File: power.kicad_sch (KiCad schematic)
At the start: 61 parts, among them J3 Conn_02x05_Odd_Even, T1 net-tie, U1 LMR54410, U2 RT9080-33GJ5, U3 TPS546D24ARVFR, U4 MIC5504

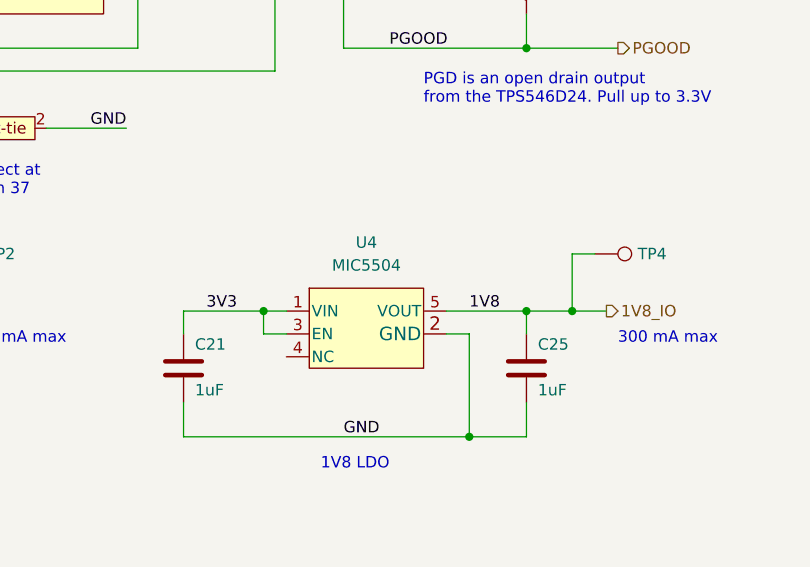
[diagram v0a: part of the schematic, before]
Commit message: finish sch rearrange for BM1368 chain
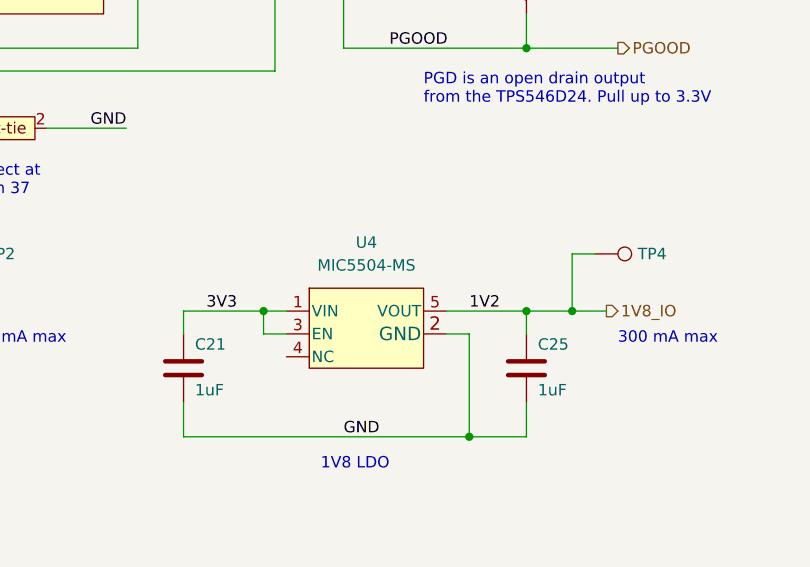
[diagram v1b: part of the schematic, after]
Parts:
- U4: value MIC5504 -> MIC5504-MS; DK 576-4879-1-ND -> C30197547; PARTNO MIC5504-1.8YM5-TR -> MIC5504-1.2YM5-TR-MS
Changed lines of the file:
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@@
 		)
 	)
-	(label "1V8"
+	(label "1V2"
 		(at 196.85 146.05 0)
 		(fields_autoplaced yes)
@@
 			)
 		)
-		(property "Value" "MIC5504"
+		(property "Value" "MIC5504-MS"
 			(at 185.42 140.97 0)
 			(effects
@@
 			)
 		)
-		(property "Datasheet" "https://www.digikey.com/en/products/detail/microchip-technology/MIC5504-1-8YM5-TR/5209404"
+		(property "Datasheet" "https://atta.szlcsc.com/upload/public/pdf/source/20240802/A85BC169CD94B58DB0326F7C46D76917.pdf"
 			(at 177.8 147.32 0)
 			(effects
@@
 			)
 		)
-		(property "DK" "576-4879-1-ND"
+		(property "DK" "C30197547"
 			(at 185.42 147.32 0)
 			(effects
@@
 			)
 		)
-		(property "PARTNO" "MIC5504-1.8YM5-TR"
+		(property "PARTNO" "MIC5504-1.2YM5-TR-MS"
 			(at 185.42 147.32 0)
 			(effects

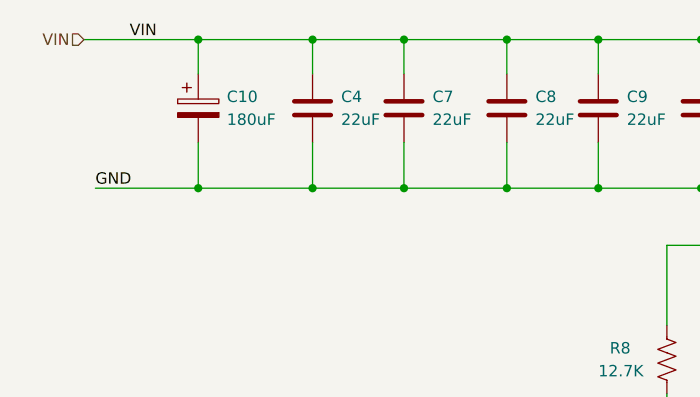
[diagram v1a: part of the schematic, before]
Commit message: Add TVS protection to avoid sudden current which may damage the TPS power regulator
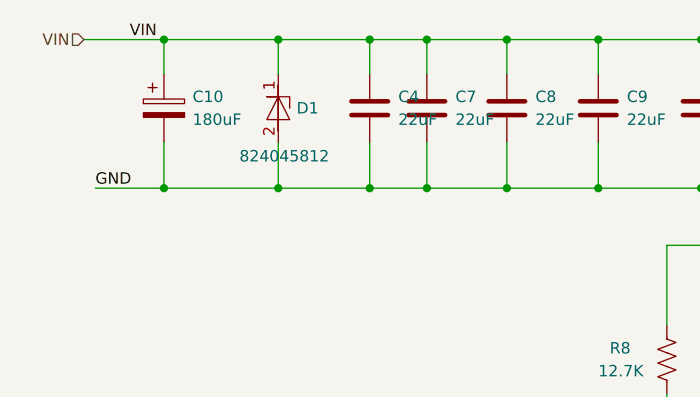
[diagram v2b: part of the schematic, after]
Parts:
- added D1: 824045812, bitaxe:824045812, symbol bitaxe:824045812
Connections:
- net GND: now also D1.2 (GND)
- net VIN: now also D1.1 (I/O)
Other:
- moved on the sheet: C10, C4, C7

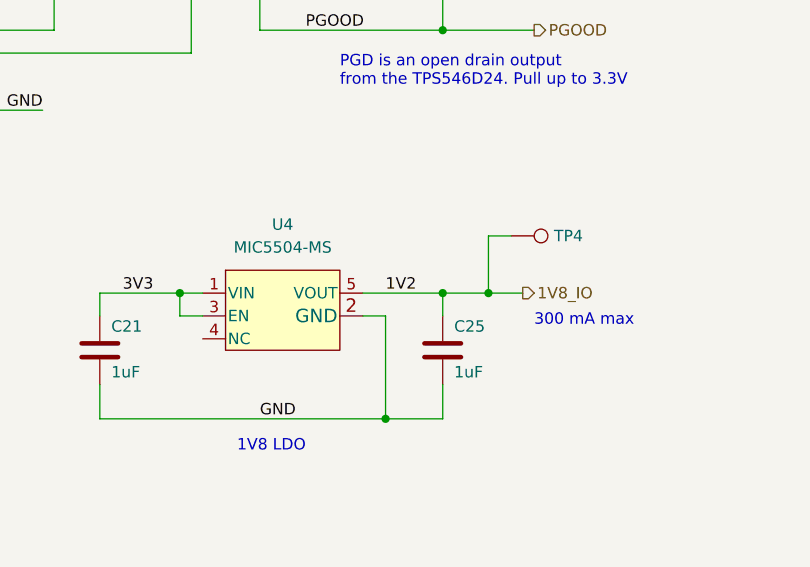
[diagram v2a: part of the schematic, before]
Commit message: Reset to 1V8
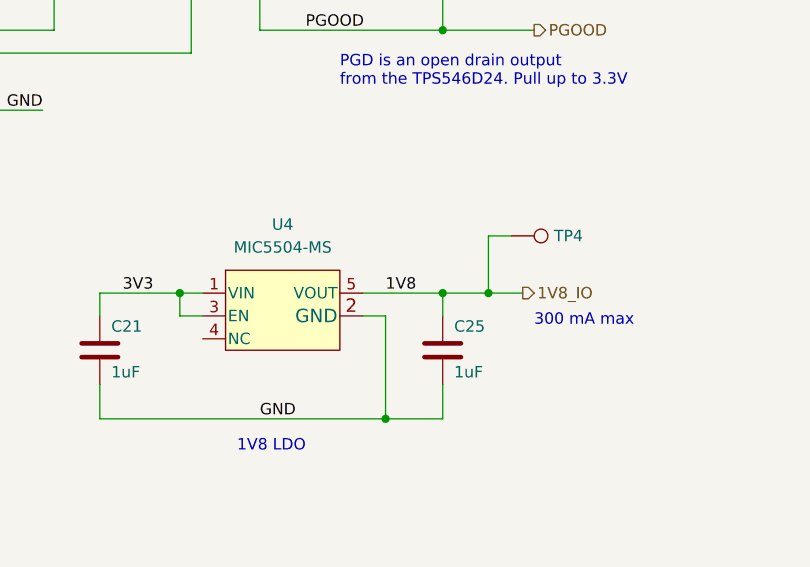
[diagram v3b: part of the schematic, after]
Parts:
- U4: DK C30197547 -> C626116; PARTNO MIC5504-1.2YM5-TR-MS -> MIC5504-1.8YM5-TR
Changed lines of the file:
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@@
 		)
 	)
-	(label "1V2"
+	(label "1V8"
 		(at 196.85 146.05 0)
 		(fields_autoplaced yes)
@@
 			)
 		)
-		(property "DK" "C30197547"
+		(property "DK" "C626116"
 			(at 185.42 147.32 0)
 			(effects
@@
 			)
 		)
-		(property "PARTNO" "MIC5504-1.2YM5-TR-MS"
+		(property "PARTNO" "MIC5504-1.8YM5-TR"
 			(at 185.42 147.32 0)
 			(effects

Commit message: upgrade board version to 703
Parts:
- added C158: 180uF, Capacitor_SMD:CP_Elec_6.3x5.9, symbol Device:C_Polarized
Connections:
- net GND: now also C158.2
- net VOUT: now also C158.1
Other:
- moved on the sheet: C29, C30
